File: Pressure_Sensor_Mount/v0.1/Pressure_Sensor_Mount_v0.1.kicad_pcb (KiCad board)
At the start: 2 copper layers, 11.9 x 8.5 mm, 2 parts, among them J1 Conn_01x04_Pin

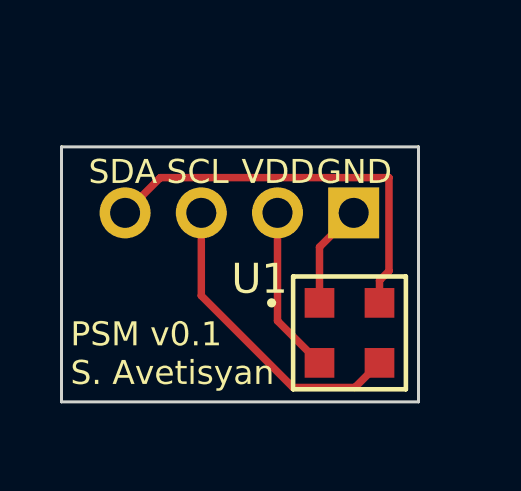
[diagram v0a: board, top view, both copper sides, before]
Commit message: Uploaded new pressure sensor mount schematic and PCB
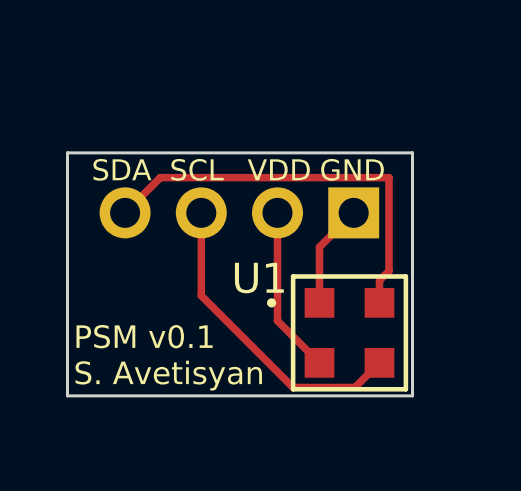
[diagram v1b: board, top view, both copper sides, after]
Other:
- board size 11.9 x 8.5 mm -> 11.5 x 8.1 mm
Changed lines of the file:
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@@
       (plot_on_all_layers_selection 0x0000000_00000000)
       (disableapertmacros false)
-      (usegerberextensions true)
-      (usegerberattributes false)
-      (usegerberadvancedattributes false)
-      (creategerberjobfile false)
+      (usegerberextensions false)
+      (usegerberattributes true)
+      (usegerberadvancedattributes true)
+      (creategerberjobfile true)
       (dashed_line_dash_ratio 12.000000)
       (dashed_line_gap_ratio 3.000000)
@@
       (psa4output false)
       (plotreference true)
-      (plotvalue false)
+      (plotvalue true)
       (plotinvisibletext false)
       (sketchpadsonfab false)
-      (subtractmaskfromsilk true)
+      (subtractmaskfromsilk false)
       (outputformat 1)
       (mirror false)
-      (drillshape 0)
+      (drillshape 1)
       (scaleselection 1)
-      (outputdirectory "./plots/")
+      (outputdirectory "")
     )
   )
@@
     (property "ki_keywords" "connector")
     (attr through_hole)
-    (fp_text reference "J1" (at -3.4 -7.94 180) (layer "B.SilkS")
-        (effects (font (size 0.8 0.8) (thickness 0.1)) (justify mirror))
+    (fp_text reference "J1" (at 1.4 1.26 180) (layer "B.SilkS")
+        (effects (font (size 0.5 0.5) (thickness 0.0625)) (justify mirror))
     )
     (fp_text value "Conn_01x04_Pin" (at -0.7 -3.74 180) (layer "B.Fab") hide
@@
     )
   )
-  (gr_rect (start 138.4 85.8) (end 150.3 94.3)
+  (gr_rect (start 138.6 86) (end 150.1 94.1)
     (stroke (width 0.1) (type default)) (fill none) (layer "Edge.Cuts"))
-  (gr_text "GND" (at 149.4 90.5) (layer "B.SilkS")
-    (effects (font (size 0.8 0.8) (thickness 0.1)) (justify left bottom mirror))
-  )
-  (gr_text "SDA" (at 141.7 90.5) (layer "B.SilkS")
-    (effects (font (size 0.8 0.8) (thickness 0.1)) (justify left bottom mirror))
-  )
-  (gr_text "SCL" (at 144.2 90.5) (layer "B.SilkS")
-    (effects (font (size 0.8 0.8) (thickness 0.1)) (justify left bottom mirror))
-  )
-  (gr_text "VDD" (at 146.7 90.5) (layer "B.SilkS")
-    (effects (font (size 0.8 0.8) (thickness 0.1)) (justify left bottom mirror))
+  (gr_text "GND" (at 149.2 90.3) (layer "B.SilkS")
+    (effects (font (size 0.7 0.7) (thickness 0.0875)) (justify left bottom mirror))
+  )
+  (gr_text "SDA" (at 141.6 90.3) (layer "B.SilkS")
+    (effects (font (size 0.7 0.7) (thickness 0.0875)) (justify left bottom mirror))
+  )
+  (gr_text "SCL" (at 144.1 90.3) (layer "B.SilkS")
+    (effects (font (size 0.7 0.7) (thickness 0.0875)) (justify left bottom mirror))
+  )
+  (gr_text "VDD" (at 146.6 90.3) (layer "B.SilkS")
+    (effects (font (size 0.7 0.7) (thickness 0.0875)) (justify left bottom mirror))
   )
   (gr_text "PSM v0.1\nS. Avetisyan" (at 150.1 93.7) (layer "B.SilkS")
     (effects (font (size 1 1) (thickness 0.15)) (justify left bottom mirror))
   )
-  (gr_text "PSM v0.1\nS. Avetisyan" (at 138.7 93.8) (layer "F.SilkS")
-    (effects (font (size 0.8 0.8) (thickness 0.1)) (justify left bottom))
-  )
-  (gr_text "VDD" (at 144.4 87.1) (layer "F.SilkS")
-    (effects (font (size 0.8 0.8) (thickness 0.1)) (justify left bottom))
-  )
-  (gr_text "SDA" (at 139.3 87.1) (layer "F.SilkS")
-    (effects (font (size 0.8 0.8) (thickness 0.1)) (justify left bottom))
-  )
-  (gr_text "GND" (at 146.9 87.1) (layer "F.SilkS")
-    (effects (font (size 0.8 0.8) (thickness 0.1)) (justify left bottom))
-  )
-  (gr_text "SCL" (at 141.9 87.1) (layer "F.SilkS")
-    (effects (font (size 0.8 0.8) (thickness 0.1)) (justify left bottom))
+  (gr_text "PSM v0.1\nS. Avetisyan" (at 138.8 93.8) (layer "F.SilkS")
+    (effects (font (size 0.75 0.75) (thickness 0.09375)) (justify left bottom))
+  )
+  (gr_text "SDA" (at 139.4 87) (layer "F.SilkS")
+    (effects (font (size 0.7 0.7) (thickness 0.0875)) (justify left bottom))
+  )
+  (gr_text "SCL" (at 142 87) (layer "F.SilkS")
+    (effects (font (size 0.7 0.7) (thickness 0.0875)) (justify left bottom))
+  )
+  (gr_text "GND" (at 147 87) (layer "F.SilkS")
+    (effects (font (size 0.7 0.7) (thickness 0.0875)) (justify left bottom))
+  )
+  (gr_text "VDD" (at 144.6 87) (layer "F.SilkS")
+    (effects (font (size 0.7 0.7) (thickness 0.0875)) (justify left bottom))
   )
   (segment (start 147 91) (end 147 89.14) (width 0.25) (layer "F.Cu") (net 1))

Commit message: Full Rework of NanoBoard Libraries, Updated Final Version of NB101
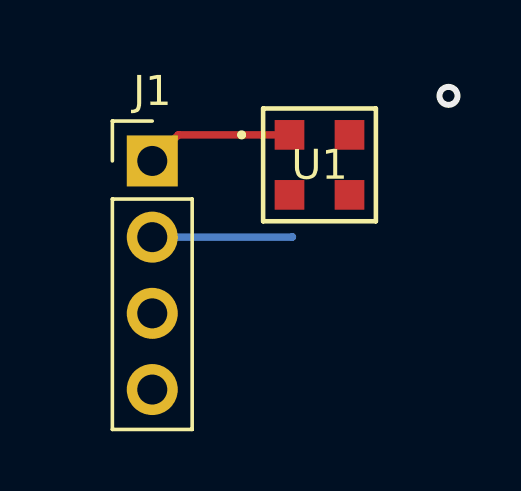
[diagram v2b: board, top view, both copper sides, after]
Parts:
- J1: moved to F.Cu
- moved J1 6.93 mm to (141.4, 86.3), turned to 0 degrees
- moved U1 5.69 mm to (147.0, 86.4)
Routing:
- net Net-(J1-Pin_4): track 13.6 -> 0.00 mm
- net Net-(J1-Pin_3): track 10.3 -> 0.00 mm
- net Net-(J1-Pin_1): track 3.47 -> 4.93 mm
- net Net-(J1-Pin_2): track 5.58 -> 4.68 mm
- net (no net): vias 0 -> 1
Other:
- board outline removed
